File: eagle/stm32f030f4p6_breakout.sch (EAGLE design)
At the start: 10 parts, among them U1 STM32F030F4PXTSSOP20

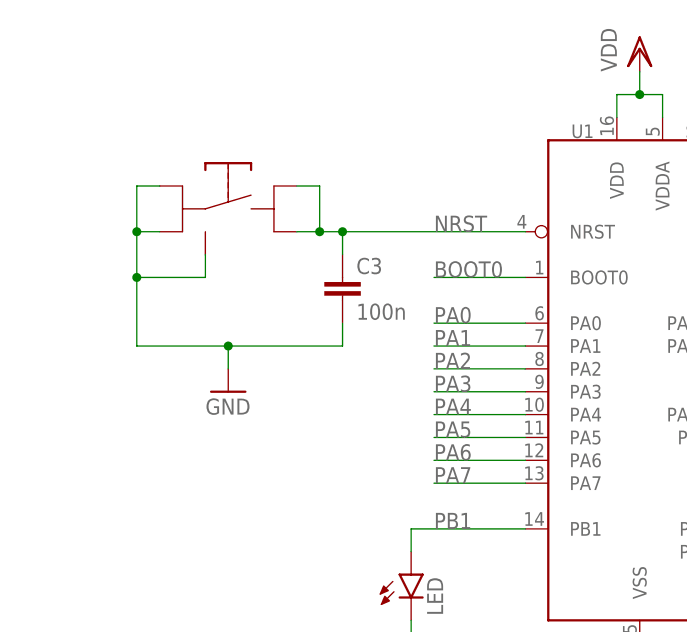
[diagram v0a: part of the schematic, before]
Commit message: - added BOOT0 pulldown - silkscreen type slightly increased to 35mil - wider supply tracks - minor changes to routing
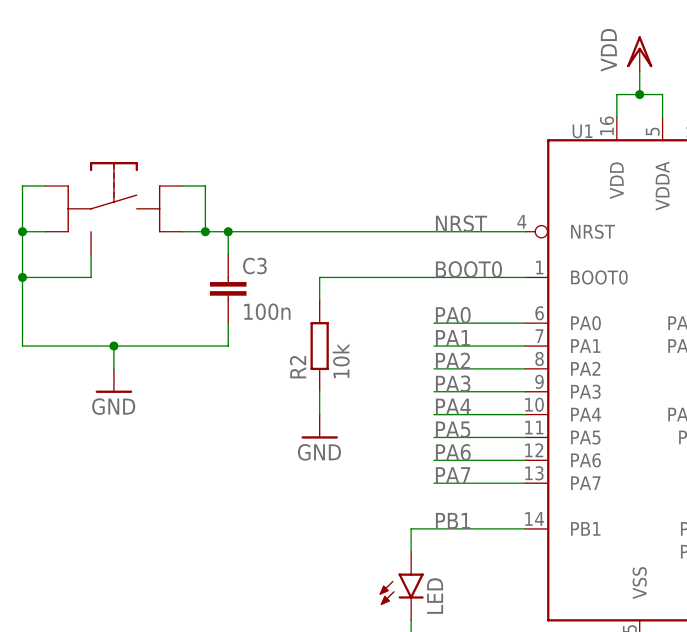
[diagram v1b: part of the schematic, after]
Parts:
- added R2: 10k, rcl_smd:R-EUR0603
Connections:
- net BOOT0: now also R2.2
- net GND: now also R2.1
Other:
- moved on the sheet: C3
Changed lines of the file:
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@@
 <part name="GND4" library="supply1" deviceset="GND" device=""/>
 <part name="GND5" library="supply1" deviceset="GND" device=""/>
+<part name="R2" library="rcl_smd" deviceset="R-EU" device="R0603" value="10k"/>
+<part name="GND6" library="supply1" deviceset="GND" device=""/>
 </parts>
 <sheets>
@@
 <instance part="U1" gate="G$1" x="0" y="-15.24"/>
 <instance part="JP3" gate="A" x="-38.1" y="53.34"/>
-<instance part="RESET" gate="G$1" x="-45.72" y="5.08" rot="MR0"/>
+<instance part="RESET" gate="G$1" x="-58.42" y="5.08" rot="MR0"/>
 <instance part="JP1" gate="A" x="17.78" y="58.42"/>
 <instance part="LED" gate="G$1" x="-25.4" y="-35.56"/>
@@
 <instance part="C2" gate="G$1" x="20.32" y="33.02"/>
 <instance part="JP2" gate="A" x="-15.24" y="53.34"/>
-<instance part="C3" gate="G$1" x="-33.02" y="-2.54"/>
+<instance part="C3" gate="G$1" x="-45.72" y="-2.54"/>
 <instance part="VDD1" gate="G$1" x="0" y="22.86"/>
 <instance part="VDD3" gate="G$1" x="15.24" y="43.18"/>
-<instance part="GND1" gate="1" x="-45.72" y="-15.24"/>
+<instance part="GND1" gate="1" x="-58.42" y="-15.24"/>
 <instance part="GND2" gate="1" x="-25.4" y="-58.42"/>
 <instance part="GND3" gate="1" x="0" y="-48.26"/>
 <instance part="GND4" gate="1" x="10.16" y="22.86"/>
 <instance part="GND5" gate="1" x="20.32" y="22.86"/>
+<instance part="R2" gate="G$1" x="-35.56" y="-10.16" rot="R90"/>
+<instance part="GND6" gate="1" x="-35.56" y="-20.32"/>
 </instances>
 <busses>
@@
 </segment>
 <segment>
-<wire x1="-55.88" y1="-2.54" x2="-55.88" y2="-10.16" width="0.1524" layer="91"/>
-<wire x1="-55.88" y1="7.62" x2="-55.88" y2="2.54" width="0.1524" layer="91"/>
-<wire x1="-55.88" y1="2.54" x2="-55.88" y2="-2.54" width="0.1524" layer="91"/>
-<junction x="-55.88" y="-2.54"/>
+<wire x1="-68.58" y1="-2.54" x2="-68.58" y2="-10.16" width="0.1524" layer="91"/>
+<wire x1="-68.58" y1="7.62" x2="-68.58" y2="2.54" width="0.1524" layer="91"/>
+<wire x1="-68.58" y1="2.54" x2="-68.58" y2="-2.54" width="0.1524" layer="91"/>
+<junction x="-68.58" y="-2.54"/>
 <pinref part="RESET" gate="G$1" pin="4"/>
-<wire x1="-48.26" y1="-2.54" x2="-55.88" y2="-2.54" width="0.1524" layer="91"/>
-<wire x1="-55.88" y1="7.62" x2="-53.34" y2="7.62" width="0.1524" layer="91"/>
+<wire x1="-60.96" y1="-2.54" x2="-68.58" y2="-2.54" width="0.1524" layer="91"/>
+<wire x1="-68.58" y1="7.62" x2="-66.04" y2="7.62" width="0.1524" layer="91"/>
 <pinref part="RESET" gate="G$1" pin="3"/>
-<wire x1="-55.88" y1="2.54" x2="-53.34" y2="2.54" width="0.1524" layer="91"/>
-<junction x="-55.88" y="2.54"/>
+<wire x1="-68.58" y1="2.54" x2="-66.04" y2="2.54" width="0.1524" layer="91"/>
+<junction x="-68.58" y="2.54"/>
 <pinref part="RESET" gate="G$1" pin="G"/>
-<wire x1="-48.26" y1="0" x2="-48.26" y2="-2.54" width="0.1524" layer="91"/>
-<wire x1="-55.88" y1="-10.16" x2="-45.72" y2="-10.16" width="0.1524" layer="91"/>
+<wire x1="-60.96" y1="0" x2="-60.96" y2="-2.54" width="0.1524" layer="91"/>
+<wire x1="-68.58" y1="-10.16" x2="-58.42" y2="-10.16" width="0.1524" layer="91"/>
 <pinref part="C3" gate="G$1" pin="2"/>
-<wire x1="-45.72" y1="-10.16" x2="-33.02" y2="-10.16" width="0.1524" layer="91"/>
-<wire x1="-33.02" y1="-10.16" x2="-33.02" y2="-7.62" width="0.1524" layer="91"/>
+<wire x1="-58.42" y1="-10.16" x2="-45.72" y2="-10.16" width="0.1524" layer="91"/>
+<wire x1="-45.72" y1="-10.16" x2="-45.72" y2="-7.62" width="0.1524" layer="91"/>
 <pinref part="GND1" gate="1" pin="GND"/>
-<wire x1="-45.72" y1="-10.16" x2="-45.72" y2="-12.7" width="0.1524" layer="91"/>
-<junction x="-45.72" y="-10.16"/>
+<wire x1="-58.42" y1="-10.16" x2="-58.42" y2="-12.7" width="0.1524" layer="91"/>
+<junction x="-58.42" y="-10.16"/>
 </segment>
 <segment>
@@
 <wire x1="-17.78" y1="43.18" x2="-30.48" y2="43.18" width="0.1524" layer="91"/>
 <label x="-30.48" y="43.18" size="1.778" layer="95"/>
+</segment>
+<segment>
+<pinref part="GND6" gate="1" pin="GND"/>
+<pinref part="R2" gate="G$1" pin="1"/>
+<wire x1="-35.56" y1="-17.78" x2="-35.56" y2="-15.24" width="0.1524" layer="91"/>
 </segment>
 </net>
@@
 <segment>
 <pinref part="U1" gate="G$1" pin="NRST"/>
-<wire x1="-12.7" y1="2.54" x2="-33.02" y2="2.54" width="0.1524" layer="91"/>
+<wire x1="-12.7" y1="2.54" x2="-45.72" y2="2.54" width="0.1524" layer="91"/>
 <label x="-22.86" y="2.54" size="1.778" layer="95"/>
 <pinref part="RESET" gate="G$1" pin="2"/>
-<wire x1="-33.02" y1="2.54" x2="-35.56" y2="2.54" width="0.1524" layer="91"/>
-<wire x1="-35.56" y1="7.62" x2="-35.56" y2="2.54" width="0.1524" layer="91"/>
-<wire x1="-38.1" y1="2.54" x2="-35.56" y2="2.54" width="0.1524" layer="91"/>
-<junction x="-35.56" y="2.54"/>
+<wire x1="-45.72" y1="2.54" x2="-48.26" y2="2.54" width="0.1524" layer="91"/>
+<wire x1="-48.26" y1="7.62" x2="-48.26" y2="2.54" width="0.1524" layer="91"/>
+<wire x1="-50.8" y1="2.54" x2="-48.26" y2="2.54" width="0.1524" layer="91"/>
+<junction x="-48.26" y="2.54"/>
 <pinref part="RESET" gate="G$1" pin="1"/>
-<wire x1="-38.1" y1="7.62" x2="-35.56" y2="7.62" width="0.1524" layer="91"/>
+<wire x1="-50.8" y1="7.62" x2="-48.26" y2="7.62" width="0.1524" layer="91"/>
 <pinref part="C3" gate="G$1" pin="1"/>
-<wire x1="-33.02" y1="0" x2="-33.02" y2="2.54" width="0.1524" layer="91"/>
-<junction x="-33.02" y="2.54"/>
+<wire x1="-45.72" y1="0" x2="-45.72" y2="2.54" width="0.1524" layer="91"/>
+<junction x="-45.72" y="2.54"/>
 </segment>
 <segment>
@@
 <segment>
 <pinref part="U1" gate="G$1" pin="BOOT0"/>
-<wire x1="-12.7" y1="-2.54" x2="-22.86" y2="-2.54" width="0.1524" layer="91"/>
 <label x="-22.86" y="-2.54" size="1.778" layer="95"/>
+<pinref part="R2" gate="G$1" pin="2"/>
+<wire x1="-12.7" y1="-2.54" x2="-35.56" y2="-2.54" width="0.1524" layer="91"/>
+<wire x1="-35.56" y1="-2.54" x2="-35.56" y2="-5.08" width="0.1524" layer="91"/>
 </segment>
 <segment>
